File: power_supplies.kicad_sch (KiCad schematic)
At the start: 55 parts, among them IC1 ECP5-BGA256, Q16 2NPN, U15 1V8REG, U3 3V3REG, U4 1V15REG, U5 2V5REG

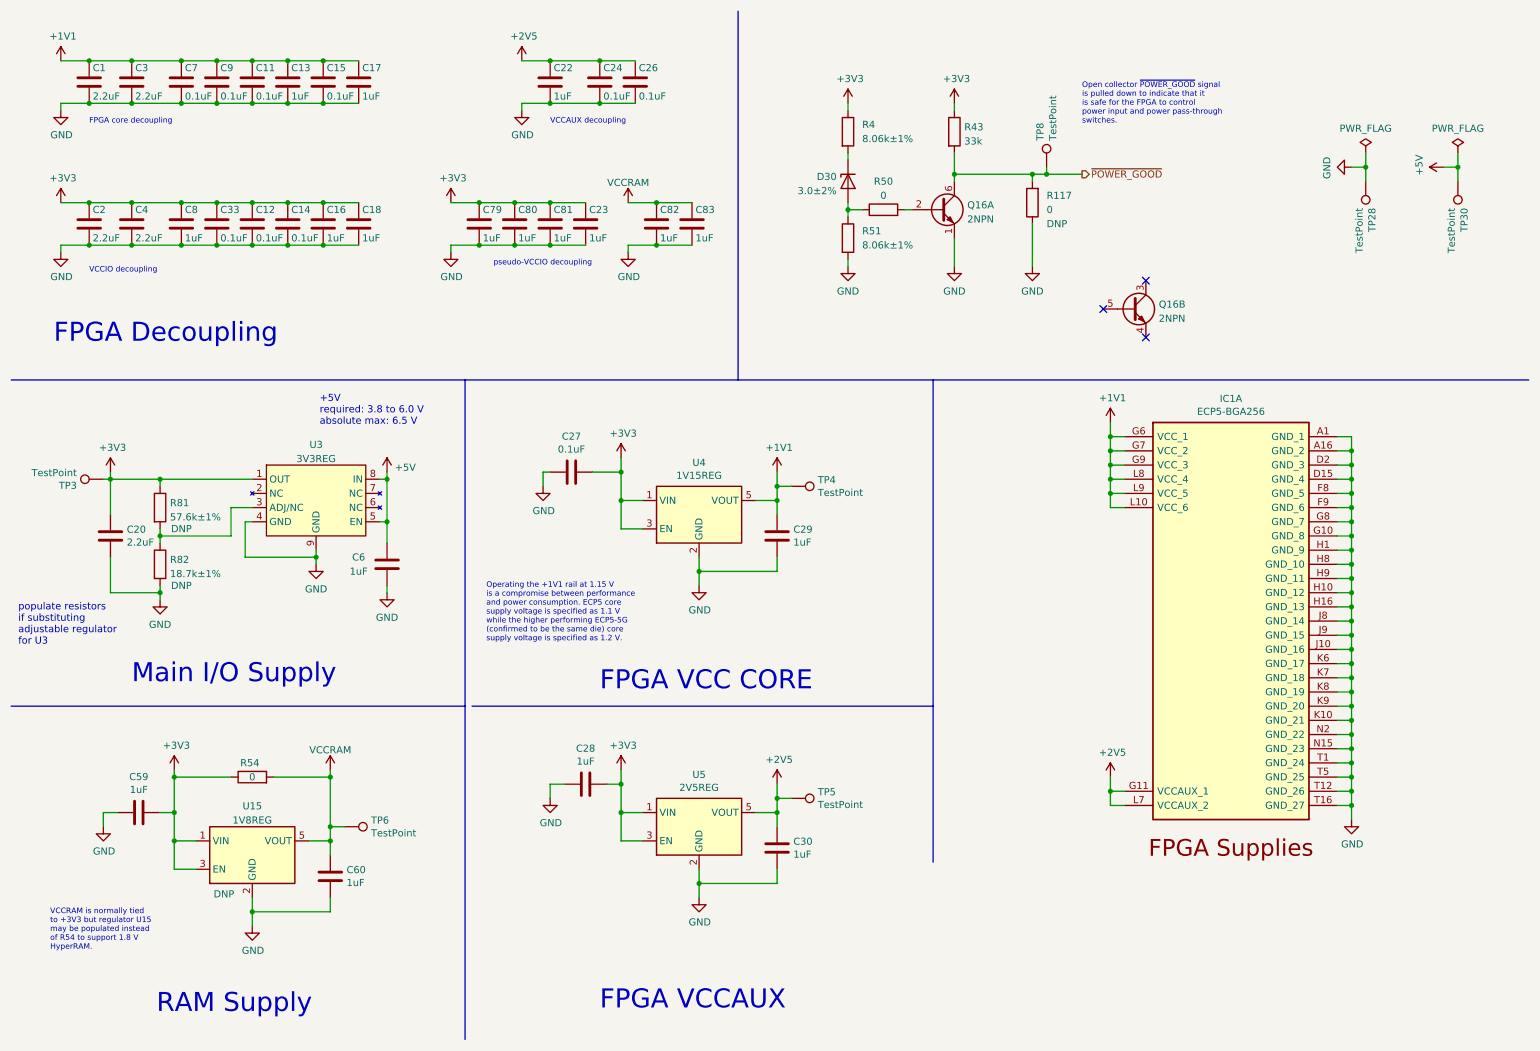
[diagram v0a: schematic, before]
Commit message: add first round of hits on lcsc
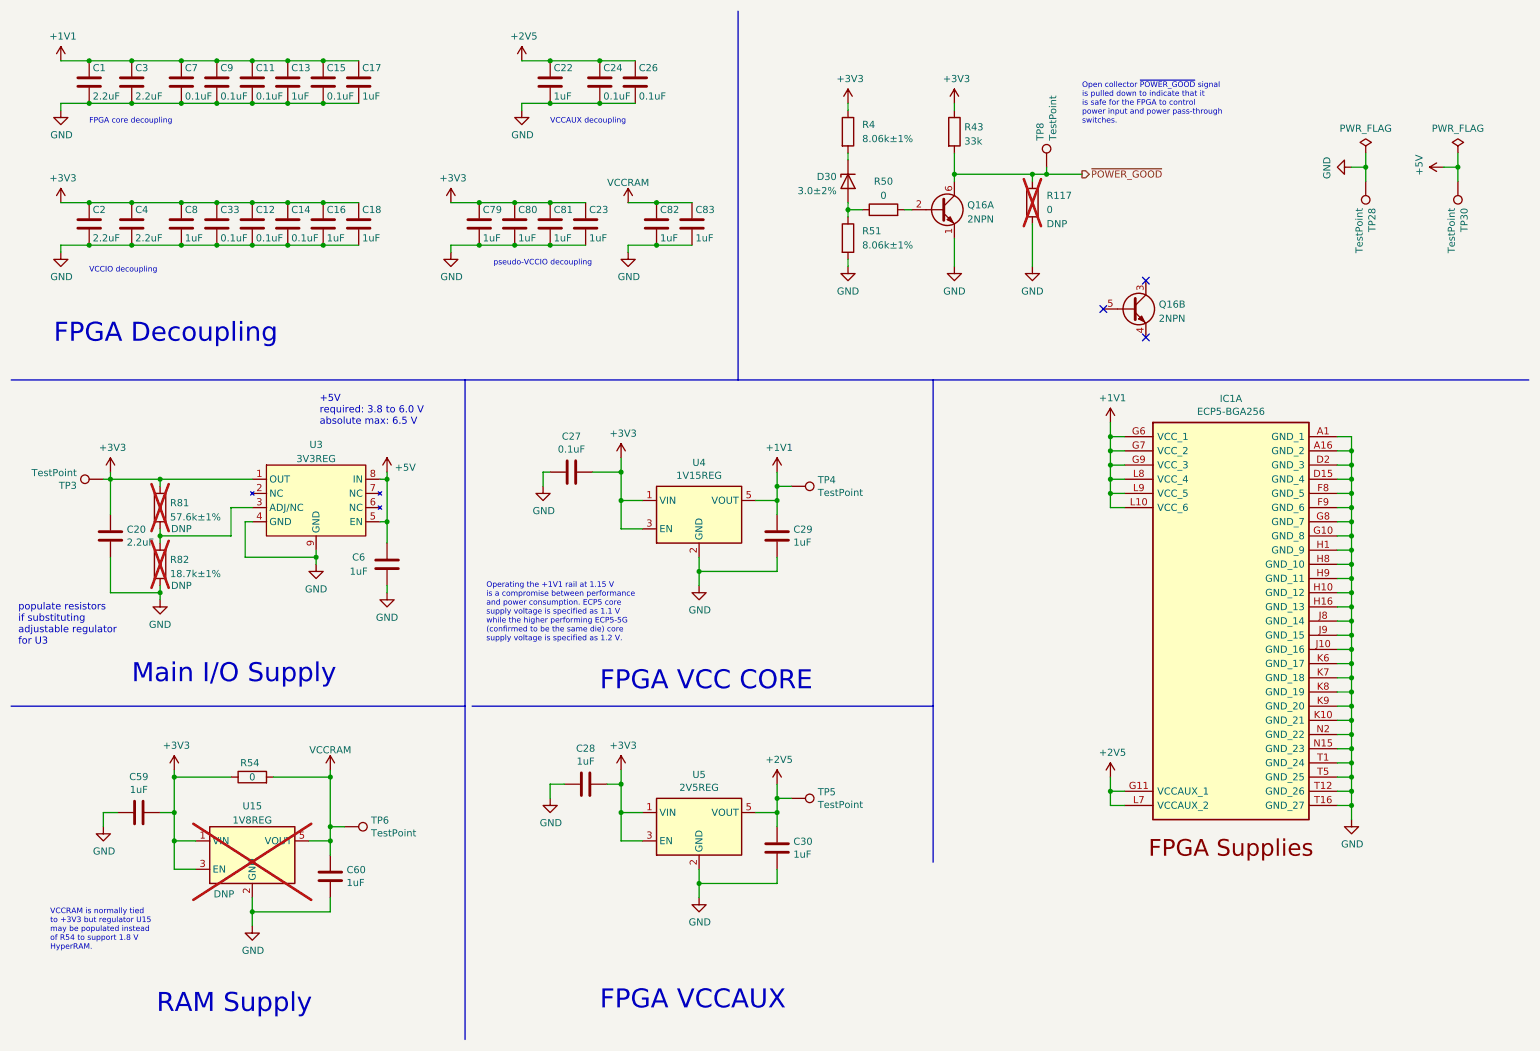
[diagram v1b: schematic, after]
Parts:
- C1, C2, C20, C3, C4: LCSC# (none) -> C1607
- C11, C12, C14, C15, C24, C26, C27, C33, C7, C9: LCSC# (none) -> C100072
- C13, C16, C17, C18, C22, C23, C28, C29, C30, C59, C6, C60, C79, C8, C80, C81, C82, C83: LCSC# (none) -> C318573
- D30: LCSC# (none) -> C551198
- Q16: LCSC# (none) -> C5380687
- R117, R81, R82, U15: now not fitted
- R4, R51: LCSC# (none) -> C2076955
- R50, R54: LCSC# (none) -> C106231
- U3: LCSC# (none) -> C151007
